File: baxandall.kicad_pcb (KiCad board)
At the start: 2 copper layers, 200 x 59 mm, 68 parts, among them P11 CONN_01X03, P11 CONN_01X04, P21 CONN_01X03, P21 CONN_01X04, P31 CONN_01X03, P31 CONN_01X04, P41 CONN_01X03, P41 CONN_01X04, U11 OP275, U21 OP275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

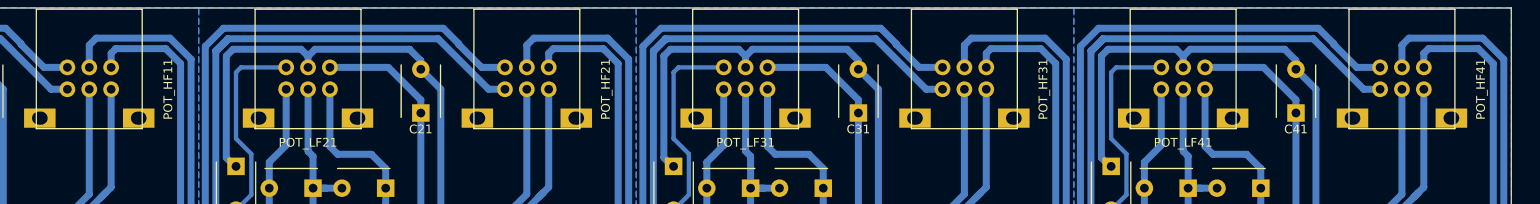
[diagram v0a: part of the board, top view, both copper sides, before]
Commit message: Updating rk09 footprint on PCB
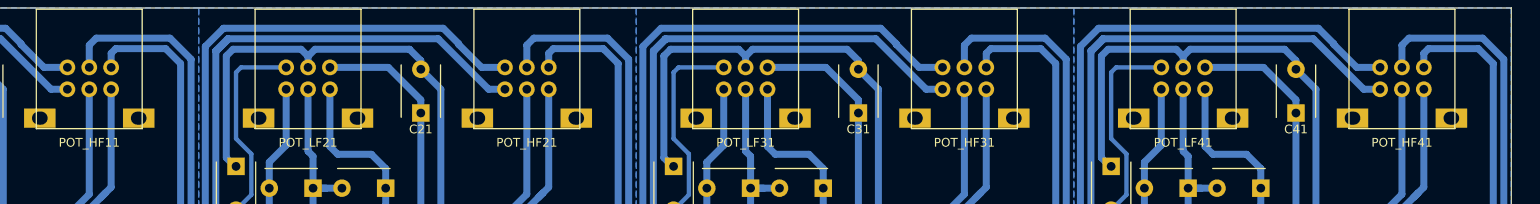
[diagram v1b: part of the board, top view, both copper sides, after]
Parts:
- POT_HF11, POT_HF21, POT_HF31, POT_HF41, POT_LF11, POT_LF21, POT_LF31, POT_LF41: footprint ALPS_pot:RK09 -> potentiometers:Potentiometer_ALPS_RK09
